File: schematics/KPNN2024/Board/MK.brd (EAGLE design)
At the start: 7.8 x 3 mm, 7 parts

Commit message: ПОМЕЛО
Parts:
- added U$2: SWITCH_MSS, UNKNOWN-2024:SWITCH_MSS
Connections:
- new net ADC0: U$1.A0
- new net D0_SD: U$1.B7
- new net SCL1: U$1.B6
- new net SDA_BME: U$1.B9
- new net SWITCH: U$1.B1, U$2.2
- net 3V3: now also U$2.3
- net CE_RADIO: now also U$1.C13; no longer U$1.C15
- net D0: no longer U$1.B7
- net GND: now also U$2.1
- net SCL: no longer U$1.B6
- net SDA: no longer U$1.B9
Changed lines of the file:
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@@
 <?xml version="1.0" encoding="utf-8"?>
 <!DOCTYPE eagle SYSTEM "eagle.dtd">
-<eagle version="9.6.2">
+<eagle version="9.6.0">
 <drawing>
 <settings>
@@
 <attribute name="VALUE" x="-46.635" y="-62.905" size="1.27" layer="27"/>
 </element>
+<element name="U$2" library="UNKNOWN-2024" package="SWITCH_MSS" value="SWITCH_MSS" x="-48" y="-69" smashed="yes">
+<attribute name="NAME" x="-51.8862" y="-66.1712" size="1.27" layer="25" ratio="10"/>
+<attribute name="VALUE" x="-51.81" y="-72.175" size="1.27" layer="27"/>
+</element>
 </elements>
 <signals>
@@
 <contactref element="U$1" pad="GND3"/>
 <contactref element="MICRO_SD" pad="VSS"/>
+<contactref element="U$2" pad="1"/>
+<wire x1="-48.05" y1="-62" x2="-50.54" y2="-69" width="0" layer="19" extent="1-1"/>
 <wire x1="-39.15" y1="-61" x2="-48.05" y2="-62" width="0" layer="19" extent="1-1"/>
 <wire x1="-23.1" y1="-40.77" x2="-39.15" y2="-61" width="0" layer="19" extent="1-1"/>
@@
 <contactref element="U$1" pad="3V3"/>
 <contactref element="MICRO_SD" pad="VDD"/>
-<wire x1="-20.9" y1="-40.77" x2="-38.81" y2="-29.67" width="0" layer="19" extent="1-1"/>
+<contactref element="U$2" pad="3"/>
+<wire x1="-20.9" y1="-40.77" x2="-45.46" y2="-69" width="0" layer="19" extent="1-1"/>
+<wire x1="-38.81" y1="-29.67" x2="-20.9" y2="-40.77" width="0" layer="19" extent="1-1"/>
 <wire x1="-4.05" y1="-20.38" x2="-20.9" y2="-40.77" width="0" layer="19" extent="1-1"/>
 <wire x1="36.59" y1="-31.81" x2="-4.05" y2="-20.38" width="0" layer="19" extent="1-1"/>
@@
 <signal name="SCL">
 <contactref element="BME280" pad="P$3"/>
-<contactref element="U$1" pad="B6"/>
-<wire x1="23.89" y1="-35.62" x2="-33.73" y2="-29.67" width="0" layer="19" extent="1-1"/>
 </signal>
 <signal name="SDA">
 <contactref element="BME280" pad="P$4"/>
-<contactref element="U$1" pad="B9"/>
-<wire x1="31.51" y1="-35.62" x2="-31.19" y2="-29.67" width="0" layer="19" extent="1-1"/>
 </signal>
 <signal name="CMD">
@@
 </signal>
 <signal name="D0">
-<contactref element="U$1" pad="B7"/>
 <contactref element="MICRO_SD" pad="DAT0"/>
-<wire x1="26.43" y1="-35.62" x2="-24.2" y2="-40.77" width="0" layer="19" extent="1-1"/>
 </signal>
 <signal name="SD_CLK">
@@
 <contactref element="U$1" pad="C14"/>
 </signal>
-<signal name="CE_RADIO">
-<contactref element="U$1" pad="C15"/>
-</signal>
 <signal name="IRQ_RADIO">
 <contactref element="U$1" pad="B8"/>
@@
 <contactref element="U$1" pad="B13"/>
 </signal>
+<signal name="ADC0">
+<contactref element="U$1" pad="A0"/>
+</signal>
+<signal name="CE_RADIO">
+<contactref element="U$1" pad="C13"/>
+</signal>
+<signal name="SDA_BME">
+<contactref element="U$1" pad="B9"/>
+</signal>
+<signal name="D0_SD">
+<contactref element="U$1" pad="B7"/>
+</signal>
+<signal name="SCL1">
+<contactref element="U$1" pad="B6"/>
+</signal>
+<signal name="SWITCH">
+<contactref element="U$1" pad="B1"/>
+<contactref element="U$2" pad="2"/>
+<wire x1="3.57" y1="-20.38" x2="-48" y2="-69" width="0" layer="19" extent="1-1"/>
+</signal>
 </signals>

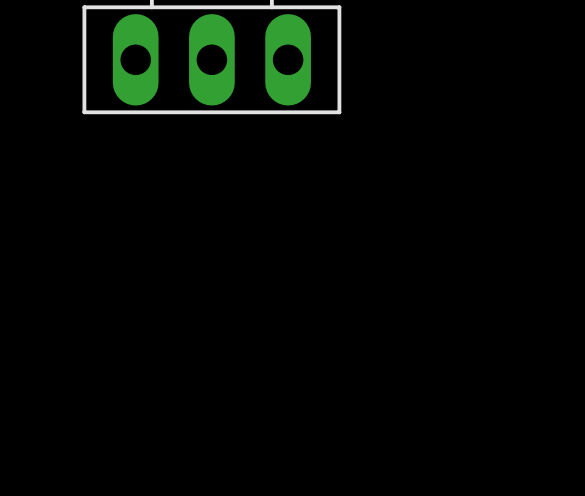
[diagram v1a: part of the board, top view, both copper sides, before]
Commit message: Добавлены УГО радио и разъемов радиолинии
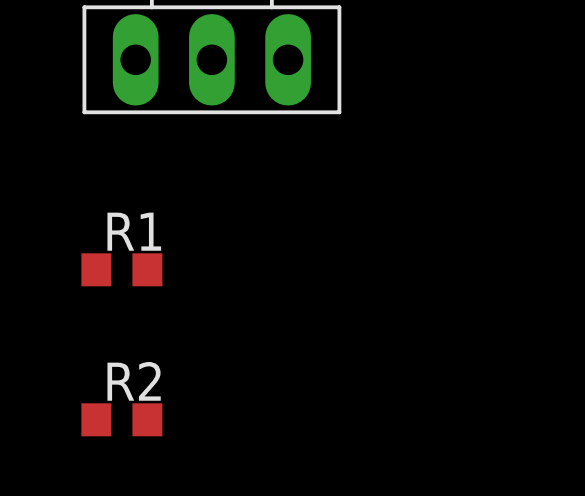
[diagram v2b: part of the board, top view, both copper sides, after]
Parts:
- added R1, R2: 10k, rcl:R0603
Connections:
- new net N$1: R1.1, U$2.3
- new net N$2: R2.1, U$2.1
- net 3V3: now also R2.2; no longer U$2.3
- net GND: now also R1.2; no longer U$2.1
- net SWITCH: no longer U$2.2
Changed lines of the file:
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@@
 <attribute name="VALUE" x="-51.81" y="-72.175" size="1.27" layer="27"/>
+</element>
+<element name="R1" library="rcl" library_urn="urn:adsk.eagle:library:334" package="R0603" package3d_urn="urn:adsk.eagle:package:23555/3" value="10k" x="-51" y="-76" smashed="yes">
+<attribute name="NAME" x="-51.635" y="-75.365" size="1.27" layer="25"/>
+<attribute name="POPULARITY" value="77" x="-51" y="-76" size="1.778" layer="27" display="off"/>
+<attribute name="SPICEPREFIX" value="R" x="-51" y="-76" size="1.778" layer="27" display="off"/>
+<attribute name="VALUE" x="-51.635" y="-77.905" size="1.27" layer="27"/>
+</element>
+<element name="R2" library="rcl" library_urn="urn:adsk.eagle:library:334" package="R0603" package3d_urn="urn:adsk.eagle:package:23555/3" value="10k" x="-51" y="-81" smashed="yes">
+<attribute name="NAME" x="-51.635" y="-80.365" size="1.27" layer="25"/>
+<attribute name="POPULARITY" value="77" x="-51" y="-81" size="1.778" layer="27" display="off"/>
+<attribute name="SPICEPREFIX" value="R" x="-51" y="-81" size="1.778" layer="27" display="off"/>
+<attribute name="VALUE" x="-51.635" y="-82.905" size="1.27" layer="27"/>
 </element>
 </elements>
@@
 <contactref element="U$1" pad="GND3"/>
 <contactref element="MICRO_SD" pad="VSS"/>
-<contactref element="U$2" pad="1"/>
-<wire x1="-48.05" y1="-62" x2="-50.54" y2="-69" width="0" layer="19" extent="1-1"/>
+<contactref element="R1" pad="2"/>
+<wire x1="-48.05" y1="-62" x2="-50.15" y2="-76" width="0" layer="19" extent="1-1"/>
 <wire x1="-39.15" y1="-61" x2="-48.05" y2="-62" width="0" layer="19" extent="1-1"/>
 <wire x1="-23.1" y1="-40.77" x2="-39.15" y2="-61" width="0" layer="19" extent="1-1"/>
@@
 <contactref element="U$1" pad="3V3"/>
 <contactref element="MICRO_SD" pad="VDD"/>
-<contactref element="U$2" pad="3"/>
-<wire x1="-20.9" y1="-40.77" x2="-45.46" y2="-69" width="0" layer="19" extent="1-1"/>
+<contactref element="R2" pad="2"/>
+<wire x1="-20.9" y1="-40.77" x2="-50.15" y2="-81" width="0" layer="19" extent="1-1"/>
 <wire x1="-38.81" y1="-29.67" x2="-20.9" y2="-40.77" width="0" layer="19" extent="1-1"/>
 <wire x1="-4.05" y1="-20.38" x2="-20.9" y2="-40.77" width="0" layer="19" extent="1-1"/>
@@
 <signal name="SWITCH">
 <contactref element="U$1" pad="B1"/>
-<contactref element="U$2" pad="2"/>
-<wire x1="3.57" y1="-20.38" x2="-48" y2="-69" width="0" layer="19" extent="1-1"/>
+</signal>
+<signal name="N$1">
+<contactref element="R1" pad="1"/>
+<contactref element="U$2" pad="3"/>
+<wire x1="-45.46" y1="-69" x2="-51.85" y2="-76" width="0" layer="19" extent="1-1"/>
+</signal>
+<signal name="N$2">
+<contactref element="R2" pad="1"/>
+<contactref element="U$2" pad="1"/>
+<wire x1="-50.54" y1="-69" x2="-51.85" y2="-81" width="0" layer="19" extent="1-1"/>
 </signal>
 </signals>

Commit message: Вабба Лабба Даб Даб
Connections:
- net ADC0 renamed ADC_FOTO
- removed net SCL1: U$1.B6
- removed net SDA_BME: U$1.B9
- net SCL: now also U$1.B6
- net SDA: now also U$1.B9
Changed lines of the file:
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@@
 <signal name="SCL">
 <contactref element="BME280" pad="P$3"/>
+<contactref element="U$1" pad="B6"/>
+<wire x1="23.89" y1="-35.62" x2="-33.73" y2="-29.67" width="0" layer="19" extent="1-1"/>
 </signal>
 <signal name="SDA">
 <contactref element="BME280" pad="P$4"/>
+<contactref element="U$1" pad="B9"/>
+<wire x1="31.51" y1="-35.62" x2="-31.19" y2="-29.67" width="0" layer="19" extent="1-1"/>
 </signal>
 <signal name="CMD">
@@
 <contactref element="U$1" pad="B13"/>
 </signal>
-<signal name="ADC0">
+<signal name="ADC_FOTO">
 <contactref element="U$1" pad="A0"/>
 </signal>
@@
 <contactref element="U$1" pad="C13"/>
 </signal>
-<signal name="SDA_BME">
-<contactref element="U$1" pad="B9"/>
-</signal>
 <signal name="D0_SD">
 <contactref element="U$1" pad="B7"/>
 </signal>
-<signal name="SCL1">
-<contactref element="U$1" pad="B6"/>
-</signal>
 <signal name="SWITCH">

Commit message: я тоже
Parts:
- moved R2 165.8 mm to (73.0, 29.0), turned to 134 degrees
- moved R1 156.8 mm to (69.0, 25.0), turned to 134 degrees
- moved U$2 153.8 mm to (76.0, 22.0), turned to 223 degrees
- moved U$20 131.6 mm to (46.0, 30.0), flipped to the bottom, turned to 180 degrees
- moved R10 124.5 mm to (43.0, 26.0), flipped to the bottom, turned to 90 degrees
- moved R9 123.0 mm to (47.0, 26.0), flipped to the bottom, turned to 90 degrees
- moved BUZZER 121.9 mm to (45.0, 28.0), turned to 180 degrees
- moved BME280 112.1 mm to (59.0, 26.0), turned to 270 degrees
- moved U$1 88.2 mm to (50.0, 53.0)
- moved MICRO_SD 69.7 mm to (26.0, 19.0), turned to 132 degrees
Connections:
- new net RX2_UART: U$1.A3
- new net TX2_UART: U$1.A2
- net SWITCH: now also U$2.2
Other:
- board size 7.8 x 3 mm -> 68.9 x 68.9 mm

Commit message: плата
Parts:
- moved BUZZER 52.5 mm to (95.0, 44.0), flipped to the bottom
- moved U$20 49.7 mm to (5.11, 1.84), turned to 270 degrees
- moved BME280 34.1 mm to (92.2, 17.8), turned to 0 degrees
- moved R9 25.2 mm to (44.0, 1.00), turned to 180 degrees
- moved R1 17.9 mm to (61.0, 9.00)
- moved MICRO_SD 13.7 mm to (16.3, 9.35)
- moved U$1 13.5 mm to (41.0, 43.0), turned to 180 degrees
- moved U$2 12.8 mm to (66.8, 13.2)
- moved R10 11.7 mm to (49.0, 16.0)
- moved R2 11.2 mm to (71.0, 18.0)
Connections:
- net BUZZER: now also U$1.A4
- net IRQ_RADIO: now also U$1.C15; no longer U$1.B8
- net MOSI_SR: now also U$1.B5
- net SCL: now also U$1.B8; no longer U$1.B6

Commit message: разъемы смд
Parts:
- added U$3: PBS_SMD_X12, UNKNOWN-2024:PBD_SMD_X12
- added U$4: PBS_SMD_X9, UNKNOWN-2024:PBS_SMD_X9
- moved U$20 98.6 mm to (95.2, 42.1), turned to 180 degrees
- moved R9 67.5 mm to (95.2, 45.0)
- moved R10 55.9 mm to (95.2, 47.4), turned to 0 degrees
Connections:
- net RX2_UART renamed RX2_BLE
- net RX_UART renamed RX1_GPS
- net TX2_UART renamed TX2_BLE
- net TX_UART renamed TX1_GPS
- new net DIR_DRIVER: U$1.A9
- new net STEP_DRIVER: U$1.A10
- new net SW_AMP: U$1.B6
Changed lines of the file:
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@@
 <?xml version="1.0" encoding="utf-8"?>
 <!DOCTYPE eagle SYSTEM "eagle.dtd">
-<eagle version="9.6.0">
+<eagle version="9.4.2">
 <drawing>
 <settings>
-<setting alwaysvectorfont="no"/>
+<setting alwaysvectorfont="yes"/>
 <setting verticaltext="up"/>
 </settings>
-<grid distance="1" unitdist="mm" unit="mm" style="lines" multiple="1" display="no" altdistance="0.003125" altunitdist="mic" altunit="mm"/>
+<grid distance="1" unitdist="mm" unit="mm" style="lines" multiple="1" display="yes" altdistance="0.1" altunitdist="mm" altunit="mm"/>
 <layers>
 <layer number="1" name="Top" color="4" fill="1" visible="yes" active="yes"/>
+<layer number="2" name="Route2" color="16" fill="1" visible="no" active="yes"/>
+<layer number="3" name="Route3" color="17" fill="1" visible="no" active="yes"/>
+<layer number="4" name="Route4" color="18" fill="1" visible="no" active="yes"/>
+<layer number="5" name="Route5" color="19" fill="1" visible="no" active="yes"/>
+<layer number="6" name="Route6" color="25" fill="1" visible="no" active="yes"/>
+<layer number="7" name="Route7" color="26" fill="1" visible="no" active="yes"/>
+<layer number="8" name="Route8" color="27" fill="1" visible="no" active="yes"/>
+<layer number="9" name="Route9" color="28" fill="1" visible="no" active="yes"/>
+<layer number="10" name="Route10" color="29" fill="1" visible="no" active="yes"/>
+<layer number="11" name="Route11" color="30" fill="1" visible="no" active="yes"/>
+<layer number="12" name="Route12" color="20" fill="1" visible="no" active="yes"/>
+<layer number="13" name="Route13" color="21" fill="1" visible="no" active="yes"/>
+<layer number="14" name="Route14" color="22" fill="1" visible="no" active="yes"/>
+<layer number="15" name="Route15" color="23" fill="1" visible="no" active="yes"/>
 <layer number="16" name="Bottom" color="1" fill="1" visible="yes" active="yes"/>
 <layer number="17" name="Pads" color="2" fill="1" visible="yes" active="yes"/>
@@
 <attribute name="NAME" x="92" y="37" size="1.27" layer="22" rot="MR180"/>
 </element>
-<element name="U$20" library="CanCubeSat" package="SOT23-3" value="SI2302CDS" x="5.105815625" y="1.8376875" smashed="yes" rot="MR270">
-<attribute name="NAME" x="7.722015625" y="3.6664875" size="1.27" layer="26" ratio="10" rot="MR0"/>
-</element>
-<element name="R9" library="rcl" library_urn="urn:adsk.eagle:library:334" package="R0603" package3d_urn="urn:adsk.eagle:package:23555/3" value="10k" x="44" y="1" smashed="yes" rot="MR180">
-<attribute name="NAME" x="43.365" y="1.365" size="1.27" layer="26" rot="MR180"/>
-<attribute name="POPULARITY" value="77" x="14" y="-15" size="1.778" layer="28" rot="MR180" display="off"/>
-<attribute name="SPICEPREFIX" value="R" x="14" y="-15" size="1.778" layer="28" rot="MR180" display="off"/>
-<attribute name="VALUE" x="43.365" y="2.905" size="1.27" layer="28" rot="MR180"/>
-</element>
-<element name="R10" library="rcl" library_urn="urn:adsk.eagle:library:334" package="R0603" package3d_urn="urn:adsk.eagle:package:23555/3" value="100R" x="49" y="16" smashed="yes" rot="MR90">
-<attribute name="NAME" x="47.635" y="14.365" size="1.27" layer="26" rot="MR90"/>
-<attribute name="POPULARITY" value="77" x="60" y="-8" size="1.778" layer="28" rot="MR90" display="off"/>
-<attribute name="SPICEPREFIX" value="R" x="60" y="-8" size="1.778" layer="28" rot="MR90" display="off"/>
-<attribute name="VALUE" x="47.095" y="15.365" size="1.27" layer="28" rot="MR90"/>
+<element name="U$20" library="CanCubeSat" package="SOT23-3" value="SI2302CDS" x="95.1623125" y="42.105815625" smashed="yes" rot="MR180">
+<attribute name="NAME" x="93.3335125" y="44.722015625" size="1.27" layer="26" ratio="10" rot="MR270"/>
+</element>
+<element name="R9" library="rcl" library_urn="urn:adsk.eagle:library:334" package="R0603" package3d_urn="urn:adsk.eagle:package:23555/3" value="10k" x="95.2" y="45" smashed="yes" rot="MR180">
+<attribute name="NAME" x="94.565" y="45.365" size="1.27" layer="26" rot="MR180"/>
+<attribute name="POPULARITY" value="77" x="65.2" y="29" size="1.778" layer="28" rot="MR180" display="off"/>
+<attribute name="SPICEPREFIX" value="R" x="65.2" y="29" size="1.778" layer="28" rot="MR180" display="off"/>
+<attribute name="VALUE" x="94.565" y="46.905" size="1.27" layer="28" rot="MR180"/>
+</element>
+<element name="R10" library="rcl" library_urn="urn:adsk.eagle:library:334" package="R0603" package3d_urn="urn:adsk.eagle:package:23555/3" value="100R" x="95.2" y="47.4" smashed="yes" rot="MR0">
+<attribute name="NAME" x="96.835" y="46.035" size="1.27" layer="26" rot="MR0"/>
+<attribute name="POPULARITY" value="77" x="119.2" y="58.4" size="1.778" layer="28" rot="MR0" display="off"/>
+<attribute name="SPICEPREFIX" value="R" x="119.2" y="58.4" size="1.778" layer="28" rot="MR0" display="off"/>
+<attribute name="VALUE" x="95.835" y="45.495" size="1.27" layer="28" rot="MR0"/>
 </element>
 <element name="U$2" library="UNKNOWN-2024" package="SWITCH_MSS" value="SWITCH_MSS" x="66.803021875" y="13.157525" smashed="yes" rot="R223">
@@
 <attribute name="VALUE" x="72.811453125" y="18.866540625" size="1.27" layer="27" rot="R134"/>
 </element>
+<element name="U$3" library="UNKNOWN-2024" package="PBD_SMD_X12" value="PBS_SMD_X12" x="44" y="64" smashed="yes"/>
+<element name="U$4" library="UNKNOWN-2024" package="PBS_SMD_X9" value="PBS_SMD_X9" x="40" y="27" smashed="yes"/>
 </elements>
 <signals>
@@
 <wire x1="24.722140625" y1="23.5478875" x2="19.41" y2="39.19" width="0" layer="19" extent="1-1"/>
 <wire x1="62.59" y1="35.38" x2="24.722140625" y2="23.5478875" width="0" layer="19" extent="1-1"/>
-<wire x1="44.85" y1="1" x2="62.59" y2="35.38" width="0" layer="19" extent="16-16"/>
-<wire x1="60.4095375" y1="9.6114375" x2="44.85" y2="1" width="0" layer="19" extent="1-16"/>
+<wire x1="96.05" y1="45" x2="62.59" y2="35.38" width="0" layer="19" extent="16-16"/>
+<wire x1="60.4095375" y1="9.6114375" x2="96.05" y2="45" width="0" layer="19" extent="1-16"/>
 <wire x1="90.891040625" y1="23.17561875" x2="60.4095375" y2="9.6114375" width="0" layer="19" extent="1-1"/>
-<wire x1="6.105815625" y1="0.8876875" x2="24.722140625" y2="23.5478875" width="0" layer="19" extent="1-16"/>
+<wire x1="96.1123125" y1="43.105815625" x2="24.722140625" y2="23.5478875" width="0" layer="19" extent="1-16"/>
 </signal>
 <signal name="N$13">
 <contactref element="U$20" pad="3"/>
 <contactref element="BUZZER" pad="P$1"/>
-<wire x1="91" y1="44" x2="4.105815625" y2="1.8376875" width="0" layer="19" extent="1-1"/>
+<wire x1="91" y1="44" x2="95.1623125" y2="41.105815625" width="0" layer="19" extent="1-1"/>
 </signal>
 <signal name="N$14">
@@
 <contactref element="R10" pad="2"/>
 <contactref element="R9" pad="1"/>
-<wire x1="49" y1="16.85" x2="6.105815625" y2="2.7876875" width="0" layer="19" extent="1-1"/>
-<wire x1="43.15" y1="1" x2="49" y2="16.85" width="0" layer="19" extent="1-1"/>
+<wire x1="94.35" y1="47.4" x2="94.2123125" y2="43.105815625" width="0" layer="19" extent="1-1"/>
+<wire x1="94.35" y1="45" x2="94.35" y2="47.4" width="0" layer="19" extent="1-1"/>
 </signal>
 <signal name="BUZZER">
 <contactref element="R10" pad="1"/>
 <contactref element="U$1" pad="A4"/>
-<wire x1="49" y1="15.15" x2="39.73" y2="35.38" width="0" layer="19" extent="16-16"/>
+<wire x1="96.05" y1="47.4" x2="39.73" y2="35.38" width="0" layer="19" extent="16-16"/>
 </signal>
 <signal name="5V">
@@
 <contactref element="U$1" pad="B4"/>
 </signal>
-<signal name="RX_UART">
-<contactref element="U$1" pad="B3"/>
-</signal>
-<signal name="TX_UART">
-<contactref element="U$1" pad="A15"/>
-</signal>
 <signal name="MISO_RADIO">
 <contactref element="U$1" pad="A11"/>
@@
 <wire x1="68.660659375" y1="14.8898" x2="71.590459375" y2="17.388559375" width="0" layer="19" extent="1-1"/>
 </signal>
-<signal name="TX2_UART">
-<contactref element="U$1" pad="A2"/>
-</signal>
-<signal name="RX2_UART">
-<contactref element="U$1" pad="A3"/>
-</signal>
 <signal name="IRQ_RADIO">
 <contactref element="U$1" pad="C15"/>
 </signal>
+<signal name="DIR_DRIVER">
+<contactref element="U$1" pad="A9"/>
+</signal>
+<signal name="STEP_DRIVER">
+<contactref element="U$1" pad="A10"/>
+</signal>
+<signal name="SW_AMP">
+<contactref element="U$1" pad="B6"/>
+</signal>
+<signal name="TX1_GPS">
+<contactref element="U$1" pad="A15"/>
+</signal>
+<signal name="RX1_GPS">
+<contactref element="U$1" pad="B3"/>
+</signal>
+<signal name="RX2_BLE">
+<contactref element="U$1" pad="A3"/>
+</signal>
+<signal name="TX2_BLE">
+<contactref element="U$1" pad="A2"/>
+</signal>
 </signals>

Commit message: разъемы еще
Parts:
- removed U$4: PBS_SMD_X9, UNKNOWN-2024:PBS_SMD_X9
- added U$5: STM32F411_BOARD, UNKNOWN-2024:STM32F411_BOARD
- U$1: value BLACKPILL -> PBS_SMD_X13; device UNKNOWN-2024:BLACKPILL -> UNKNOWN-2024:PBD_SMD_X13
- U$3: value PBS_SMD_X12 -> PBS_SMD_X9; device UNKNOWN-2024:PBD_SMD_X12 -> UNKNOWN-2024:PBS_SMD_X9
- moved U$1 43.9 mm to (23.0, 3.00), turned to 0 degrees
- moved U$3 32.6 mm to (38.0, 32.0)
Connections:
- removed net CMD: MICRO_SD.CMD, U$1.A6
- removed net RX1_GPS: U$1.B3
- removed net RX2_BLE: U$1.A3
- removed net SD_CLK: MICRO_SD.CLK, U$1.B15
- removed net TX1_GPS: U$1.A15
- removed net TX2_BLE: U$1.A2
- new net CMD_SD: MICRO_SD.CMD, U$5.12
- new net RX1_BLE: U$1.4, U$5.31
- new net RX2_GPS: U$3.8, U$5.9
- new net SD_CK: MICRO_SD.CLK, U$5.24
- new net TX1_BLE: U$1.3, U$5.30
- new net TX2_GPS: U$3.7, U$5.8
- net 3V3: now also U$1.13, U$5.1, U$5.18, U$5.40; no longer U$1.3V3, U$1.3V31, U$1.3V32
- net 5V: now also U$1.11, U$5.20, U$5.38; no longer U$1.5V, U$1.5V1
- net ADC_FOTO: now also U$1.10, U$5.6; no longer U$1.A0
- net BUZZER: now also U$5.14; no longer U$1.A4
- net CE_RADIO: now also U$3.1, U$5.2; no longer U$1.C13
- net CS_RADIO: now also U$3.2, U$5.3; no longer U$1.C14
- net D0_SD: now also U$5.35; no longer U$1.B7
- net DIR_DRIVER: now also U$1.1, U$5.26; no longer U$1.A9
- net GND: now also U$1.12, U$5.19, U$5.39; no longer U$1.GND, U$1.GND1, U$1.GND3
- net IRQ_RADIO: now also U$3.3, U$5.4; no longer U$1.C15
- net LATCH_SR: now also U$1.5, U$5.21; no longer U$1.B2
- net MISO_RADIO: now also U$3.5, U$5.28; no longer U$1.A11
- net MISO_SR: now also U$1.8, U$5.32; no longer U$1.B4
- net MOSI_RADIO: now also U$3.4, U$5.7; no longer U$1.A1
- net MOSI_SR: now also U$1.9, U$5.33; no longer U$1.A7, U$1.B5
- net OE_SR: now also U$1.6, U$5.23; no longer U$1.B10
- net SCK_RADIO: now also U$3.6, U$5.22; no longer U$1.B13
- net SCK_SR: now also U$1.7, U$5.11; no longer U$1.A5
- net SCL: now also U$5.36; no longer U$1.B8
- net SDA: now also U$5.37; no longer U$1.B9
- net STEP_DRIVER: now also U$1.2, U$5.27; no longer U$1.A10
- net SWITCH: now also U$5.15; no longer U$1.B1
- net SW_AMP: now also U$3.9, U$5.10; no longer U$1.B6
